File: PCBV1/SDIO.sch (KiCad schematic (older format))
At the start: 0 parts

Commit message: Made comments and some circuits.
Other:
- note added: "Place uSD Card holder for booting Linux"
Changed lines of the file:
@@
 $Descr A4 11693 8268
 encoding utf-8
-Sheet 6 9
+Sheet 4 8
 Title "Smart Mirror"
 Date "2021-01-21"
@@
 Comment4 ""
 $EndDescr
+Text Notes 4850 3050 0    50   ~ 0
+Place uSD Card holder for booting Linux
 $EndSCHEMATC

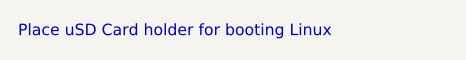
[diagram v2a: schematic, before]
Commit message: Merge of recent changes to default master (#2)
* Made a bunch of very small changes.

* Added UART, modifications to video etc.

* Minor adjustments with video connections.

* Finished video signals, added HDMI and SD connectors.
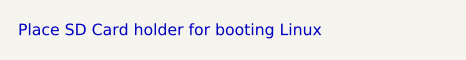
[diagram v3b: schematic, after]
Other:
- note added: "Place SD Card holder for booting Linux"
- note removed: "Place uSD Card holder for booting Linux"
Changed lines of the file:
@@
 $Descr A4 11693 8268
 encoding utf-8
-Sheet 4 8
+Sheet 3 9
 Title "Smart Mirror"
 Date "2021-01-21"
@@
 $EndDescr
 Text Notes 4850 3050 0    50   ~ 0
-Place uSD Card holder for booting Linux
+Place SD Card holder for booting Linux
 $EndSCHEMATC
